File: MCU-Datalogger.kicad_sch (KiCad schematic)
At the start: 23 parts, among them U1 24LC1025, U2 24LC1025, U3 DS1337S_, U4 ATMEGA328P-AU, Y1 Crystal, Y2 Crystal

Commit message: positioning
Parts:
- added D2: LED, symbol Device:LED
- added R7: R, symbol Device:R
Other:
- moved on the sheet: BT1, C1, C2, C3, C4, C5, D1, H1, H2, H3, H4, R1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

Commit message: component values
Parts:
- C1, C5: value C -> 0.1uF
- C2: value C_Polarized -> 100nF
- C3, C4: value C -> 22pF
- R1, R2: value R -> 4.7K
- R3, R7: value R -> 330
- R4, R5, R6: value R -> 10K
- Y1: value Crystal -> 32.768 KHz
- Y2: value Crystal -> 16 MHz
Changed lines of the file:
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@@
 			)
 		)
-		(property "Value" "R"
+		(property "Value" "4.7K"
 			(at 100.33 153.6699 0)
 			(effects
@@
 			)
 		)
-		(property "Value" "Crystal"
+		(property "Value" "32.768 KHz"
 			(at 31.75 60.9599 90)
 			(effects
@@
 			)
 		)
-		(property "Value" "R"
+		(property "Value" "10K"
 			(at 97.79 50.7999 0)
 			(effects
@@
 			)
 		)
-		(property "Value" "C"
+		(property "Value" "22pF"
 			(at 124.46 119.3799 0)
 			(effects
@@
 			)
 		)
-		(property "Value" "R"
+		(property "Value" "4.7K"
 			(at 89.6777 153.5989 0)
 			(effects
@@
 			)
 		)
-		(property "Value" "Crystal"
+		(property "Value" "16 MHz"
 			(at 139.7 110.4899 90)
 			(effects
@@
 			)
 		)
-		(property "Value" "R"
+		(property "Value" "330"
 			(at 120.65 90.17 90)
 			(effects
@@
 			)
 		)
-		(property "Value" "C_Polarized"
+		(property "Value" "100nF"
 			(at 200.66 90.5509 0)
 			(effects
@@
 			)
 		)
-		(property "Value" "R"
+		(property "Value" "10K"
 			(at 137.16 125.73 90)
 			(effects
@@
 			)
 		)
-		(property "Value" "C"
+		(property "Value" "0.1uF"
 			(at 135.89 73.66 90)
 			(effects
@@
 			)
 		)
-		(property "Value" "R"
+		(property "Value" "10K"
 			(at 88.1223 50.8709 0)
 			(effects
@@
 			)
 		)
-		(property "Value" "C"
+		(property "Value" "22pF"
 			(at 124.46 107.9499 0)
 			(effects
@@
 			)
 		)
-		(property "Value" "C"
+		(property "Value" "0.1uF"
 			(at 109.22 50.7999 0)
 			(effects
@@
 			)
 		)
-		(property "Value" "R"
+		(property "Value" "330"
 			(at 195.58 116.8399 0)
 			(effects

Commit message: footprints
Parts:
- BT1: footprint (none) -> Connector_PinHeader_2.54mm:PinHeader_1x02_P2.54mm_Vertical
- C1, C2, C3, C4, C5: footprint (none) -> Capacitor_SMD:C_0805_2012Metric
- D1, D2: footprint (none) -> LED_SMD:LED_0805_2012Metric
- H1, H2, H3, H4: footprint (none) -> MountingHole:MountingHole_2.1mm
- R1, R2, R3, R4, R5, R6, R7: footprint (none) -> Resistor_SMD:R_0805_2012Metric
- U1, U2: footprint (none) -> Package_SO:SOIC-8_3.9x4.9mm_P1.27mm
- U3: footprint DS1337S_:SOIC127P600X175-8N -> Footprints:SOIC127P600X175-8N
- U4: footprint ATMEGA328P-AU:QFP80P900X900X120-32N -> Footprints:QFP80P900X900X120-32N
- Y1, Y2: footprint (none) -> Crystal:Crystal_SMD_5032-2Pin_5.0x3.2mm_HandSoldering
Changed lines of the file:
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@@
 			)
 		)
-		(property "Footprint" ""
+		(property "Footprint" "Resistor_SMD:R_0805_2012Metric"
 			(at 96.012 152.4 90)
 			(effects
@@
 			)
 		)
-		(property "Footprint" ""
+		(property "Footprint" "Crystal:Crystal_SMD_5032-2Pin_5.0x3.2mm_HandSoldering"
 			(at 27.94 59.69 0)
 			(effects
@@
 			)
 		)
-		(property "Footprint" ""
+		(property "Footprint" "Connector_PinHeader_2.54mm:PinHeader_1x02_P2.54mm_Vertical"
 			(at 207.01 88.646 90)
 			(effects
@@
 			)
 		)
-		(property "Footprint" ""
+		(property "Footprint" "Resistor_SMD:R_0805_2012Metric"
 			(at 93.472 49.53 90)
 			(effects
@@
 			)
 		)
-		(property "Footprint" ""
+		(property "Footprint" "LED_SMD:LED_0805_2012Metric"
 			(at 137.16 95.25 0)
 			(effects
@@
 			)
 		)
-		(property "Footprint" "DS1337S_:SOIC127P600X175-8N"
+		(property "Footprint" "Footprints:SOIC127P600X175-8N"
 			(at 59.69 57.15 0)
 			(effects
@@
 			)
 		)
-		(property "Footprint" "ATMEGA328P-AU:QFP80P900X900X120-32N"
+		(property "Footprint" "Footprints:QFP80P900X900X120-32N"
 			(at 163.83 107.95 0)
 			(effects
@@
 			)
 		)
-		(property "Footprint" ""
+		(property "Footprint" "Capacitor_SMD:C_0805_2012Metric"
 			(at 121.6152 121.92 0)
 			(effects
@@
 			)
 		)
-		(property "Footprint" ""
+		(property "Footprint" "Package_SO:SOIC-8_3.9x4.9mm_P1.27mm"
 			(at 69.85 151.13 0)
 			(effects
@@
 			)
 		)
-		(property "Footprint" ""
+		(property "Footprint" "Resistor_SMD:R_0805_2012Metric"
 			(at 85.3597 152.329 90)
 			(effects
@@
 			)
 		)
-		(property "Footprint" ""
+		(property "Footprint" "Crystal:Crystal_SMD_5032-2Pin_5.0x3.2mm_HandSoldering"
 			(at 135.89 109.22 0)
 			(effects
@@
 			)
 		)
-		(property "Footprint" ""
+		(property "Footprint" "Resistor_SMD:R_0805_2012Metric"
 			(at 120.65 95.758 90)
 			(effects
@@
 			)
 		)
-		(property "Footprint" ""
+		(property "Footprint" "MountingHole:MountingHole_2.1mm"
 			(at 246.38 130.81 0)
 			(effects
@@
 			)
 		)
-		(property "Footprint" ""
+		(property "Footprint" "MountingHole:MountingHole_2.1mm"
 			(at 246.38 138.43 0)
 			(effects
@@
 			)
 		)
-		(property "Footprint" ""
+		(property "Footprint" "Capacitor_SMD:C_0805_2012Metric"
 			(at 197.8152 93.98 0)
 			(effects
@@
 			)
 		)
-		(property "Footprint" ""
+		(property "Footprint" "MountingHole:MountingHole_2.1mm"
 			(at 246.38 146.05 0)
 			(effects
@@
 			)
 		)
-		(property "Footprint" ""
+		(property "Footprint" "Resistor_SMD:R_0805_2012Metric"
 			(at 137.16 131.318 90)
 			(effects
@@
 			)
 		)
-		(property "Footprint" ""
+		(property "Footprint" "Capacitor_SMD:C_0805_2012Metric"
 			(at 139.7 77.7748 0)
 			(effects
@@
 			)
 		)
-		(property "Footprint" ""
+		(property "Footprint" "Resistor_SMD:R_0805_2012Metric"
 			(at 83.8043 49.601 90)
 			(effects
@@
 			)
 		)
-		(property "Footprint" ""
+		(property "Footprint" "LED_SMD:LED_0805_2012Metric"
 			(at 193.04 104.14 0)
 			(effects
@@
 			)
 		)
-		(property "Footprint" ""
+		(property "Footprint" "Capacitor_SMD:C_0805_2012Metric"
 			(at 121.6152 110.49 0)
 			(effects
@@
 			)
 		)
-		(property "Footprint" ""
+		(property "Footprint" "Capacitor_SMD:C_0805_2012Metric"
 			(at 106.3752 53.34 0)
 			(effects
@@
 			)
 		)
-		(property "Footprint" ""
+		(property "Footprint" "Package_SO:SOIC-8_3.9x4.9mm_P1.27mm"
 			(at 40.64 151.13 0)
 			(effects
@@
 			)
 		)
-		(property "Footprint" ""
+		(property "Footprint" "MountingHole:MountingHole_2.1mm"
 			(at 246.38 153.67 0)
 			(effects
@@
 			)
 		)
-		(property "Footprint" ""
+		(property "Footprint" "Resistor_SMD:R_0805_2012Metric"
 			(at 191.262 115.57 90)
 			(effects

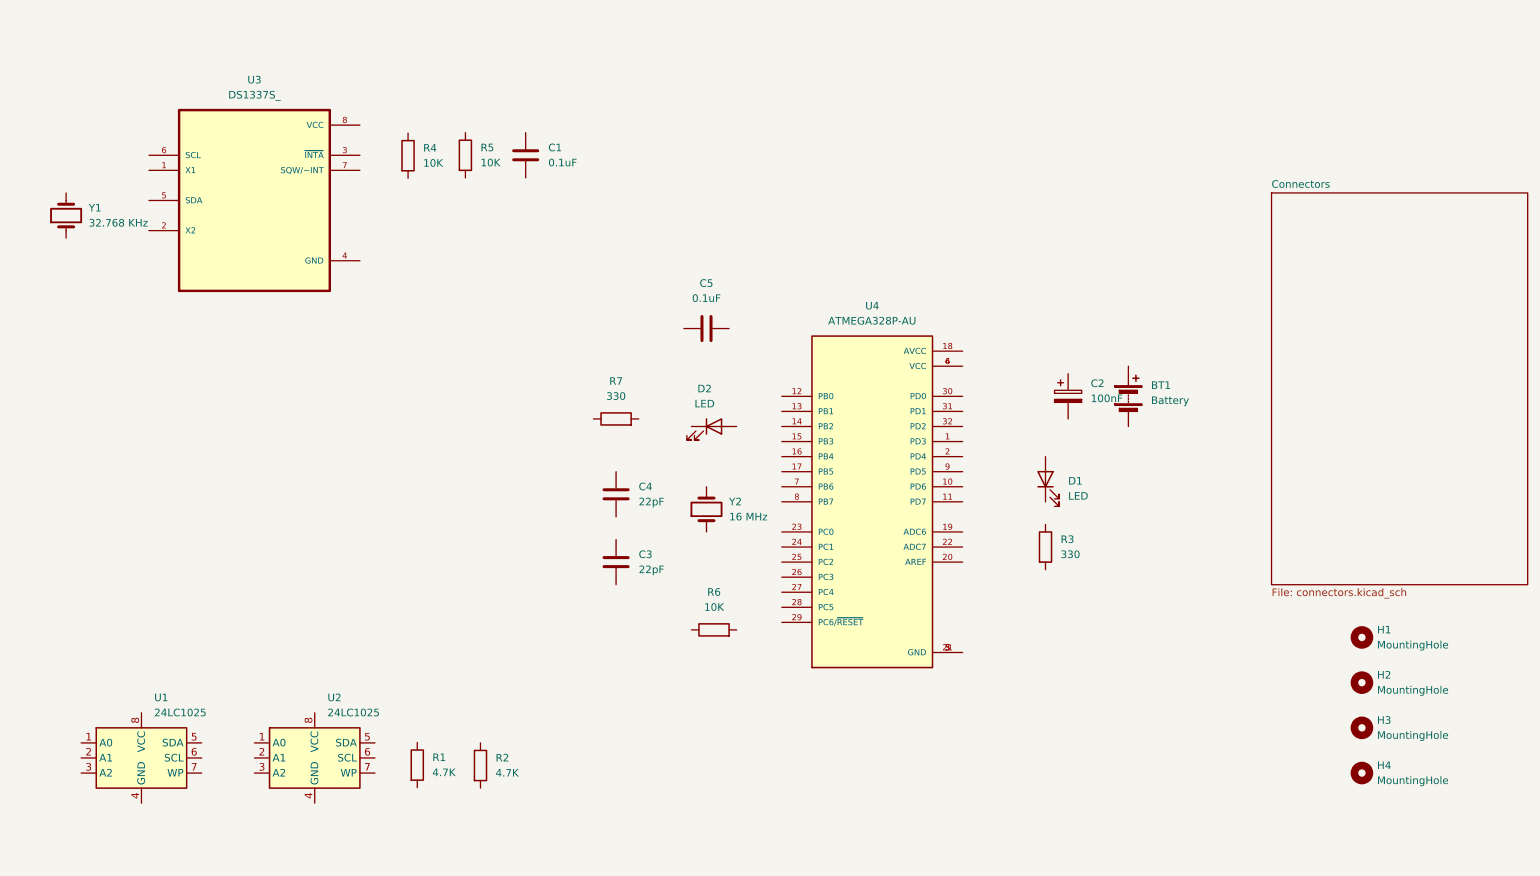
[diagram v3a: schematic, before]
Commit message: schematic wiring
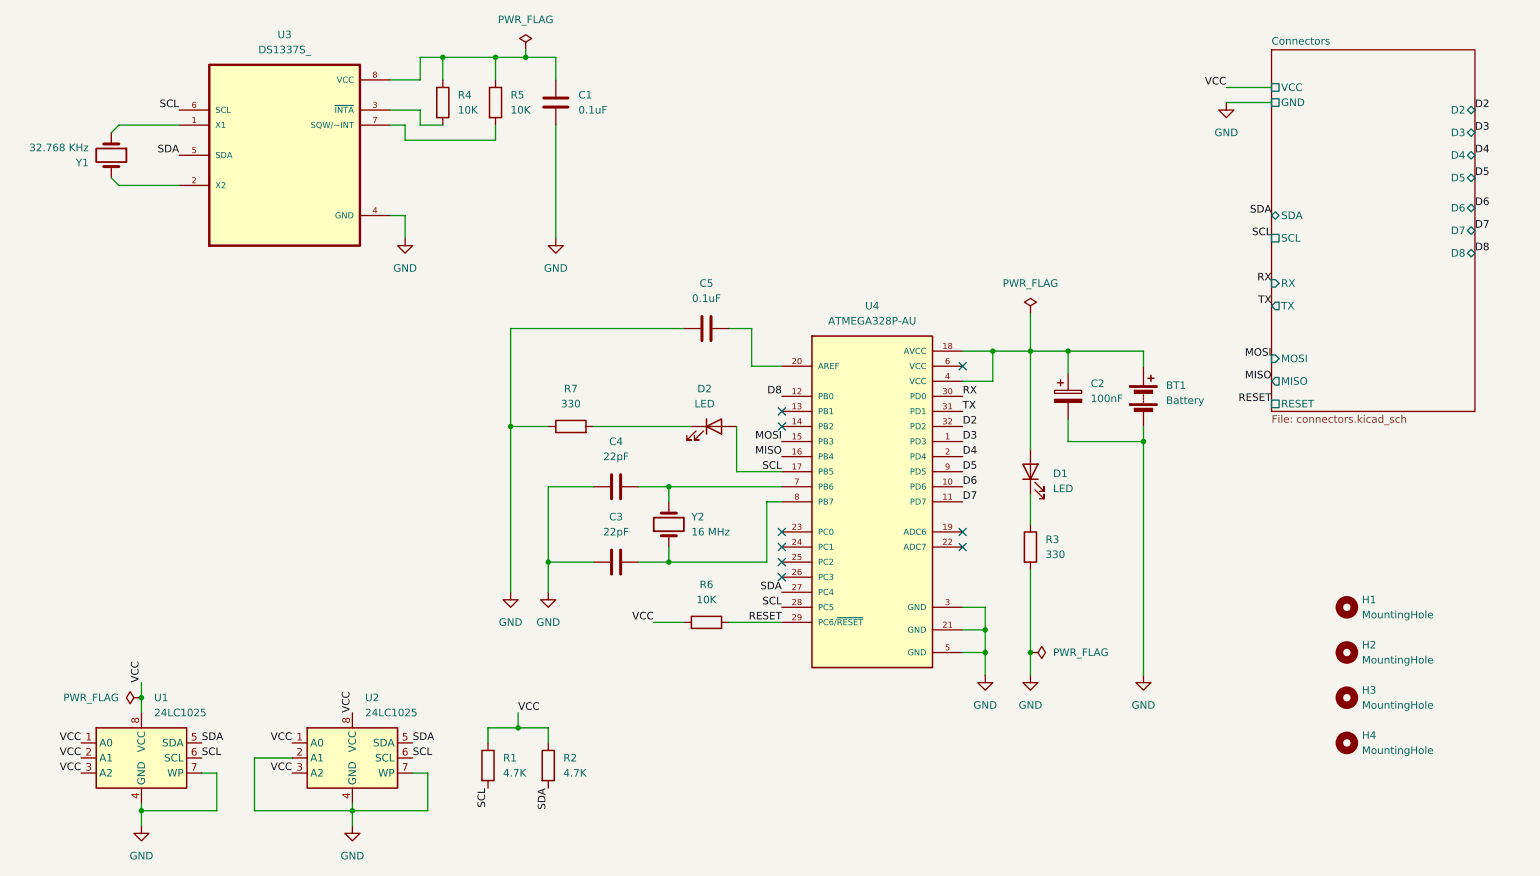
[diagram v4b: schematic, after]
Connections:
- net VCC: now reaches R2.1
- net VCC: now also R1.1, R6.1, U1.1 (A0), U1.2 (A1), U1.3 (A2), U1.8 (VCC), U2.1 (A0), U2.3 (A2), U2.8 (VCC)
- net SDA: now reaches R2.2
- net SDA: now also U1.5 (SDA), U2.5 (SDA), U3.5 (SDA), U4.27 (PC4)
- net at Y1.1: now also U3.1 (X1)
- net at Y1.2: now also U3.2 (X2)
- net at BT1.1 (+): now also C2.1, D1.2 (A), U4.18 (AVCC), U4.4 (VCC)
- net GND: now reaches BT1.2 (-)
- net GND: now also C1.2, C2.2, C3.1, C4.1, C5.1, R3.2, R7.1, U1.4 (GND), U1.7 (WP), U2.2 (A1), U2.4 (GND), U2.7 (WP), U3.4 (GND), U4.21 (GND), U4.3 (GND), U4.5 (GND)
- net at R5.1: now also C1.1, R4.1, U3.8 (VCC)
- net at R5.2: now also U3.7 (SQW/~INT)
- net at D2.1 (K): now also R7.2
- net SCL: now reaches D2.2 (A)
- net SCL: now also R1.2, U1.6 (SCL), U2.6 (SCL), U3.6 (SCL), U4.17 (PB5), U4.28 (PC5)
- net at U3.3 (~{INTA}): now also R4.2
- net D3: now reaches U4.1 (PD3)
- net D6: now reaches U4.10 (PD6)
- net D7: now reaches U4.11 (PD7)
- net D8: now reaches U4.12 (PB0)
- net MOSI: now reaches U4.15 (PB3)
- net MISO: now reaches U4.16 (PB4)
- net D4: now reaches U4.2 (PD4)
- net at U4.20 (AREF): now also C5.2
- net RESET: now reaches U4.29 (PC6/~{RESET})
- net RESET: now also R6.2
- net RX: now reaches U4.30 (PD0)
- net TX: now reaches U4.31 (PD1)
- net D2: now reaches U4.32 (PD2)
- net at U4.6 (VCC): no longer U4.4 (VCC)
- net at U4.7 (PB6): now also C4.2, Y2.2
- net at U4.8 (PB7): now also C3.2, Y2.1
- net D5: now reaches U4.9 (PD5)
- net at D1.1 (K): now also R3.1
- no-connect marks 0 -> 9
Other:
- sheet Connectors ports: added D2, D3, D4, D5, D6, D7, D8, GND, MISO, MOSI, RESET, RX, SCL, SDA, TX, VCC; removed none
- moved on the sheet: BT1, C1, C3, C4, D1, H1, H2, H3, H4, R1, R2, R3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
